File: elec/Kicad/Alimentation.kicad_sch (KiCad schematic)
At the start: 30 parts, among them Q1 SI2323DS-T1, Q4 SI2323DS-T1, SW4 SW_ON/OFF

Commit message: push de magouille pour charles
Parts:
- removed Q4: SI2323DS-T1, Package_TO_SOT_SMD:SOT-23, symbol Transistor_FET:AO3401A
- added D7: 1N4148WS, Diode_SMD:D_SOD-323, symbol Diode:1N4148WS
- R12: value 10 -> 110K
- R18: value 10 -> 300K
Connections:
- net Vbat: now also R12.2
- net VinBat: now also D7.2 (A)
- net at Q1.3 (D), SW4.1 (A): now also D7.1 (K)
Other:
- note added: "MOSFET N-Channel: Si une tension appliqué a la Gate est suppérieur que celle a la Source, le courant va circuler du Drain a la Source"
- note added: "MOSFET P-Channel: Si une tension appliqué a la Gate est inférieur a celle de la Source, le courant va circuler de la Source au Drain"
- note added: "Quand Vbat = 3.5V, BAT_PERCENT = 2.55V Quand Vbat = 4.2V, BAT_PERCENT = 3.07V"
- note removed: "PAS LE BON TYPE DE MOSFET"
- moved on the sheet: R12, R18, SW4

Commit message: va falloir faire le PCB soon
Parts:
- added JP2: USB_ID, symbol Jumper:SolderJumper_2_Open
- added JP2: USB_SHIELD, symbol Jumper:SolderJumper_2_Open
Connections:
- net GND: now also JP2.1 (A), JP2.2 (B)
- net at J?.4 (ID): now also JP2.2 (B)
- net at J?.6 (Shield): now also JP2.1 (A)
- no-connect marks 2 -> 0
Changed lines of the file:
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@@
 	)
 	(junction
+		(at 171.45 50.8)
+		(diameter 0)
+		(color 0 0 0 0)
+	)
+	(junction
 		(at 44.45 57.15)
 		(diameter 0)
@@
 	)
 	(junction
+		(at 176.53 50.8)
+		(diameter 0)
+		(color 0 0 0 0)
+	)
+	(junction
 		(at 104.14 52.07)
 		(diameter 0)
@@
 		(color 0 0 0 0)
 	)
-	(no_connect
-		(at 161.29 49.53)
-	)
-	(no_connect
-		(at 171.45 43.18)
-	)
 	(wire
 		(pts
@@
 	(wire
 		(pts
+			(xy 168.91 55.88) (xy 171.45 55.88)
+		)
+		(stroke
+			(width 0)
+			(type default)
+		)
+	)
+	(wire
+		(pts
 			(xy 115.57 52.07) (xy 125.73 52.07)
 		)
@@
 	(wire
 		(pts
-			(xy 163.83 50.8) (xy 195.58 50.8)
+			(xy 163.83 50.8) (xy 171.45 50.8)
 		)
 		(stroke
@@
 	(wire
 		(pts
+			(xy 171.45 43.18) (xy 176.53 43.18)
+		)
+		(stroke
+			(width 0)
+			(type default)
+		)
+	)
+	(wire
+		(pts
 			(xy 104.14 67.31) (xy 104.14 71.12)
 		)
@@
 	(wire
 		(pts
+			(xy 176.53 50.8) (xy 195.58 50.8)
+		)
+		(stroke
+			(width 0)
+			(type default)
+		)
+	)
+	(wire
+		(pts
 			(xy 100.33 134.62) (xy 113.03 134.62)
 		)
@@
 		)
 	)
+	(wire
+		(pts
+			(xy 171.45 50.8) (xy 176.53 50.8)
+		)
+		(stroke
+			(width 0)
+			(type default)
+		)
+	)
 	(polyline
 		(pts
@@
 	(wire
 		(pts
-			(xy 161.29 48.26) (xy 161.29 49.53)
+			(xy 161.29 48.26) (xy 161.29 55.88)
 		)
 		(stroke
@@
 	(wire
 		(pts
+			(xy 171.45 55.88) (xy 171.45 50.8)
+		)
+		(stroke
+			(width 0)
+			(type default)
+		)
+	)
+	(wire
+		(pts
 			(xy 91.44 160.02) (xy 91.44 161.29)
 		)
@@
 	)
 	(symbol
+		(lib_id "Jumper:SolderJumper_2_Open")
+		(at 176.53 46.99 90)
+		(unit 1)
+		(exclude_from_sim yes)
+		(in_bom no)
+		(on_board yes)
+		(dnp no)
+		(property "Reference" "JP2"
+			(at 181.61 46.736 0)
+			(effects
+				(font
+					(size 1.27 1.27)
+				)
+			)
+		)
+		(property "Value" "USB_ID"
+			(at 179.07 46.482 0)
+			(effects
+				(font
+					(size 1.27 1.27)
+				)
+			)
+		)
+		(property "Footprint" ""
+			(at 176.53 46.99 0)
+			(effects
+				(font
+					(size 1.27 1.27)
+				)
+				(hide yes)
+			)
+		)
+		(property "Datasheet" "~"
+			(at 176.53 46.99 0)
+			(effects
+				(font
+					(size 1.27 1.27)
+				)
+				(hide yes)
+			)
+		)
+		(property "Description" "Solder Jumper, 2-pole, open"
+			(at 176.53 46.99 0)
+			(effects
+				(font
+					(size 1.27 1.27)
+				)
+				(hide yes)
+			)
+		)
+		(pin "2"
+		)
+		(pin "1"
+		)
+		(instances
+			(project "rulerSchematic"
+				(path "/a1545928-1195-40b9-b3c4-78f837012afb/47f0fc71-ff78-496f-bb04-036a9aeaa71c/6f59428e-8e72-4854-8d86-784df1ffb46d"
+					(reference "JP2")
+					(unit 1)
+				)
+			)
+		)
+	)
+	(symbol
 		(lib_id "Device:R")
 		(at 236.22 113.03 180)
@@
 					(unit 1)
 				)
+			)
+		)
+	)
+	(symbol
+		(lib_id "Jumper:SolderJumper_2_Open")
+		(at 165.1 55.88 0)
+		(unit 1)
+		(exclude_from_sim yes)
+		(in_bom no)
+		(on_board yes)
+		(dnp no)
+		(property "Reference" "JP2"
+			(at 165.354 60.96 0)
+			(effects
+				(font
+					(size 1.27 1.27)
+				)
+			)
+		)
+		(property "Value" "USB_SHIELD"
+			(at 165.608 58.42 0)
+			(effects
+				(font
+					(size 1.27 1.27)
+				)
+			)
+		)
+		(property "Footprint" ""
+			(at 165.1 55.88 0)
+			(effects
+				(font
+					(size 1.27 1.27)
+				)
+				(hide yes)
+			)
+		)
+		(property "Datasheet" "~"
+			(at 165.1 55.88 0)
+			(effects
+				(font
+					(size 1.27 1.27)
+				)
+				(hide yes)
+			)
+		)
+		(property "Description" "Solder Jumper, 2-pole, open"
+			(at 165.1 55.88 0)
+			(effects
+				(font
+					(size 1.27 1.27)
+				)
+				(hide yes)
+			)
+		)
+		(pin "2"
+		)
+		(pin "1"
+		)
+		(instances
+			(project ""
+				(path "/a1545928-1195-40b9-b3c4-78f837012afb/47f0fc71-ff78-496f-bb04-036a9aeaa71c/6f59428e-8e72-4854-8d86-784df1ffb46d"
+					(reference "JP2")
+					(unit 1)
+				)

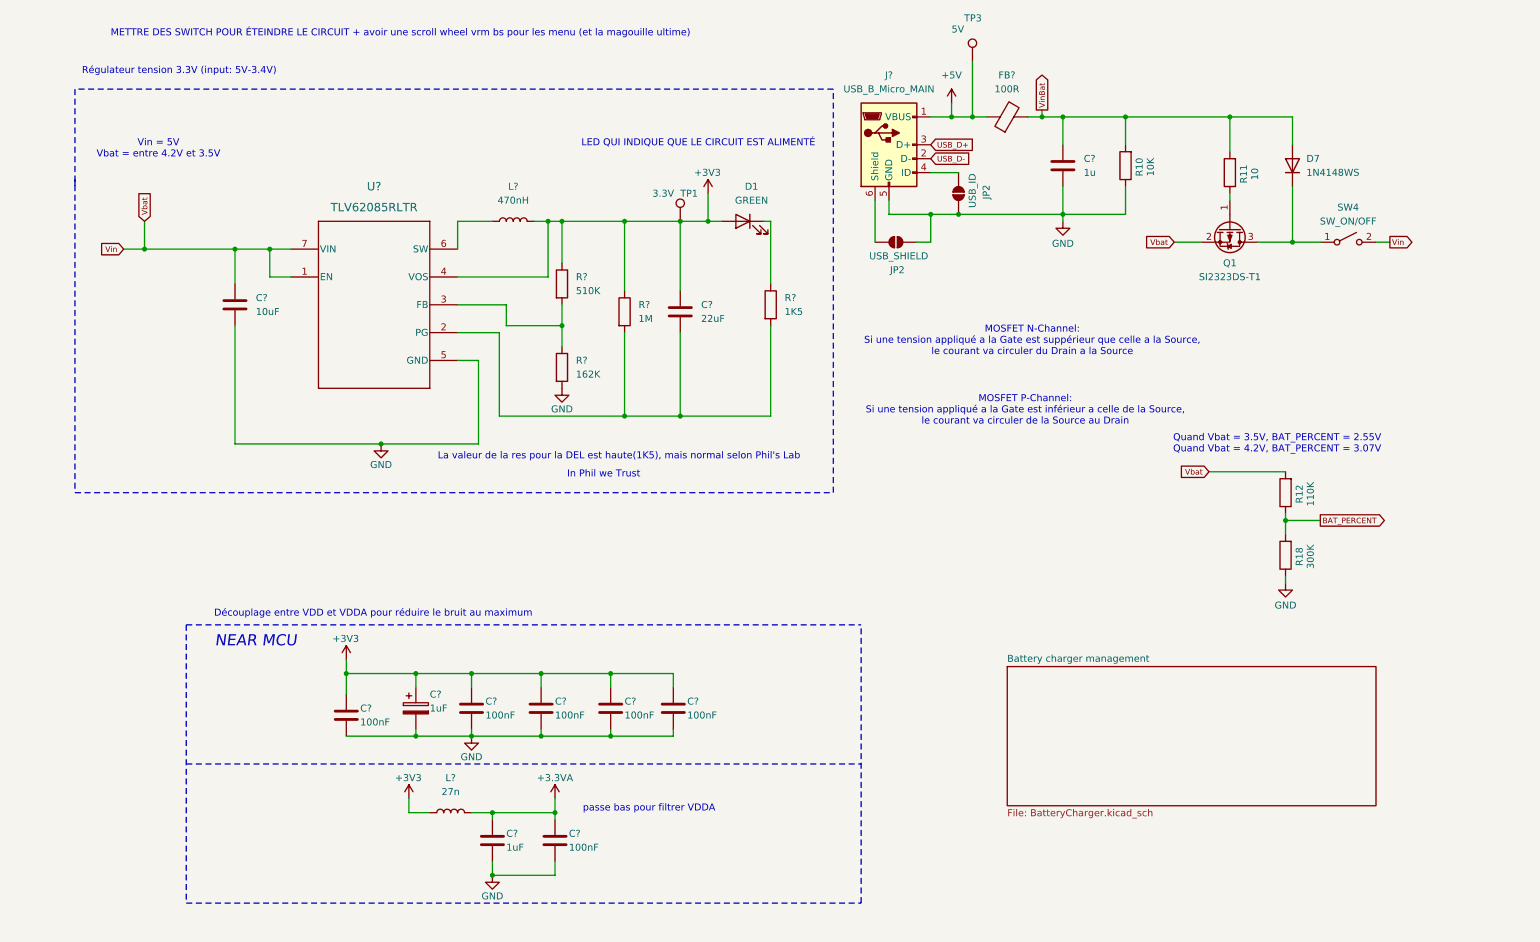
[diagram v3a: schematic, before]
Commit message: add a few footprint
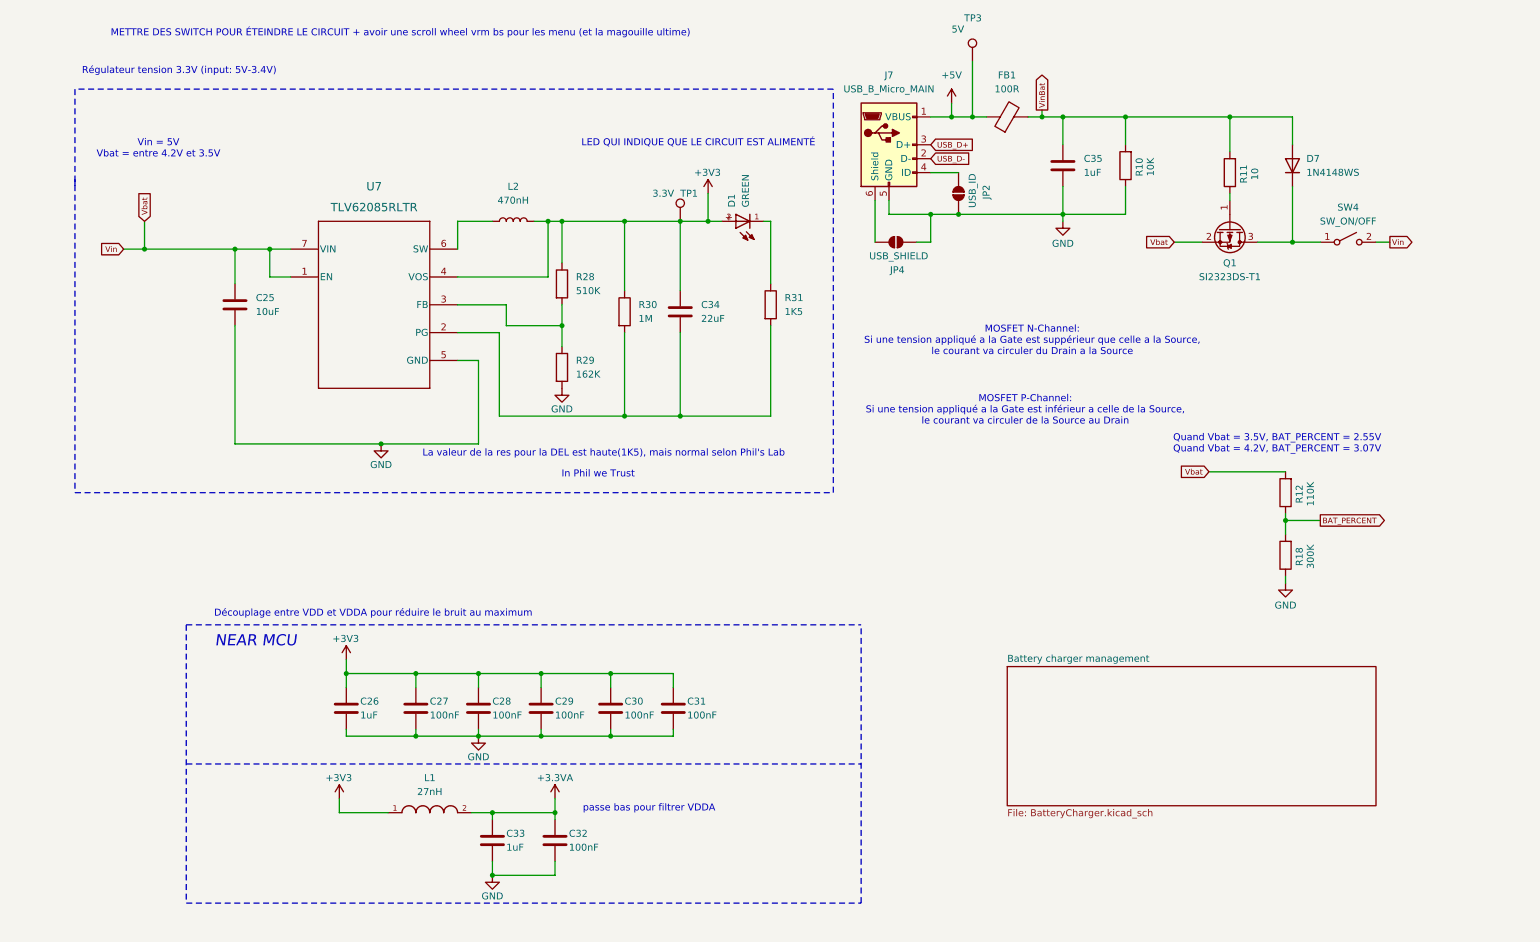
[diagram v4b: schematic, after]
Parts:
- removed C? (x4): 100nF, symbol Device:C
- removed C?: 1uF, symbol Device:C_Polarized
- removed D1: GREEN, symbol Device:LED
- removed JP2: USB_SHIELD, symbol Jumper:SolderJumper_2_Open
- removed L?: 27n, symbol Device:L
- added C26: 1uF, Capacitor_SMD:C_0603_1608Metric_Pad1.08x0.95mm_HandSolder, symbol Device:C
- added C27, C29, C30, C31: 100nF, Capacitor_SMD:C_0603_1608Metric_Pad1.08x0.95mm_HandSolder, symbol Device:C
- added D1: GREEN, SMD_LED_0603:WL-SMCD_0603, symbol WL-SMCD_0603:WL-SMCD_0603
- added JP4: USB_SHIELD, Jumper:SolderJumper-2_P1.3mm_Open_TrianglePad1.0x1.5mm, symbol Jumper:SolderJumper_2_Open
- added L1: 27nH, LQP03TN27NJ02D:INDC0603X33N, symbol LQP03TN27NJ02D:LQP03TN27NJ02D
- C25, C28, C32, C33, C34: renamed from C?; footprint (none) -> Capacitor_SMD:C_0603_1608Metric_Pad1.08x0.95mm_HandSolder
- C35: renamed from C?; value 1u -> 1uF; footprint (none) -> Capacitor_SMD:C_0603_1608Metric_Pad1.08x0.95mm_HandSolder
- FB1: renamed from FB?; footprint (none) -> SMD_FERRITE_BEAD_BLM18EG101TN1D:BEADC1608X65N
- J7: renamed from J?; footprint (none) -> Connector_USB:USB_Micro-B_Amphenol_10103594-0001LF_Horizontal
- JP2: footprint (none) -> Jumper:SolderJumper-2_P1.3mm_Open_TrianglePad1.0x1.5mm
- L2: renamed from L?; footprint (none) -> VLS252012HBX_R47M_1:IND_VLS252012HBX-R47M-1
- R10, R11, R12, R18: footprint (none) -> Resistor_SMD:R_0603_1608Metric_Pad0.98x0.95mm_HandSolder
- R28, R29, R30, R31: renamed from R?; footprint (none) -> Resistor_SMD:R_0603_1608Metric_Pad0.98x0.95mm_HandSolder
- SW4: footprint (none) -> SINGLE_DIP_SWITCH:SW_DS04-254-2-01BK-SMT
- TP1, TP3: footprint (none) -> TestPoint:TestPoint_Loop_D1.80mm_Drill1.0mm_Beaded
- U7: renamed from U?; footprint RLT0007A -> TLV62085RLTR:RLT0007A
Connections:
- net +3.3VA: now also L1.2
- net +3V3: now also C26.1, C27.1, C29.1, C30.1, C31.1, D1.2, L1.1
- net GND: now also C26.2, C27.2, C29.2, C30.2, C31.2, JP4.2 (B)
- net at R31.1: now also D1.1
- net at J7.6 (Shield): now also JP4.1 (A)
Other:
- moved on the sheet: C28

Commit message: formation torture
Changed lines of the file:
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@@
-	)
-	(symbol
-		(lib_id "power:+3.3VA")
-		(at 102.87 157.48 0)
-		(unit 1)
-		(exclude_from_sim no)
-		(in_bom yes)
-		(on_board yes)
-		(dnp no)
-		(property "Reference" "#PWR0111"
-			(at 102.87 161.29 0)
-			(effects
-				(font
-					(size 1.27 1.27)
-				)
-				(hide yes)
-			)
-		)
-		(property "Value" "+3.3VA"
-			(at 102.87 153.67 0)
-			(effects
-				(font
-					(size 1.27 1.27)
-				)
-			)
-		)
-		(property "Footprint" ""
-			(at 102.87 157.48 0)
-			(effects
-				(font
-					(size 1.27 1.27)
-				)
-				(hide yes)
-			)
-		)
-		(property "Datasheet" ""
-			(at 102.87 157.48 0)
-			(effects
-				(font
-					(size 1.27 1.27)
-				)
-				(hide yes)
-			)
-		)
-		(property "Description" ""
-			(at 102.87 157.48 0)
-			(effects
-				(font
-					(size 1.27 1.27)
-				)
-				(hide yes)
-			)
-		)
-		(pin "1"
-		)
-		(instances
-			(project "rulerSchematic"
-				(path "/a1545928-1195-40b9-b3c4-78f837012afb/47f0fc71-ff78-496f-bb04-036a9aeaa71c/6f59428e-8e72-4854-8d86-784df1ffb46d"
-					(reference "#PWR0111")
-					(unit 1)
-				)
-			)
-		)
 	)
 	(symbol
@@
 					(unit 1)
 				)
+			)
+		)
+	)
+	(symbol
+		(lib_name "+3.3VA_1")
+		(lib_id "power:+3.3VA")
+		(at 102.87 157.48 0)
+		(unit 1)
+		(exclude_from_sim no)
+		(in_bom yes)
+		(on_board yes)
+		(dnp no)
+		(fields_autoplaced yes)
+		(property "Reference" "#PWR051"
+			(at 102.87 161.29 0)
+			(effects
+				(font
+					(size 1.27 1.27)
+				)
+				(hide yes)
+			)
+		)
+		(property "Value" "+3.3VA"
+			(at 102.87 152.4 0)
+			(effects
+				(font
+					(size 1.27 1.27)
+				)
+			)
+		)
+		(property "Footprint" ""
+			(at 102.87 157.48 0)
+			(effects
+				(font
+					(size 1.27 1.27)
+				)
+				(hide yes)
+			)
+		)
+		(property "Datasheet" ""
+			(at 102.87 157.48 0)
+			(effects
+				(font
+					(size 1.27 1.27)
+				)
+				(hide yes)
+			)
+		)
+		(property "Description" "Power symbol creates a global label with name \"+3.3VA\""
+			(at 102.87 157.48 0)
+			(effects
+				(font
+					(size 1.27 1.27)
+				)
+				(hide yes)
+			)
+		)
+		(pin "1"
+		)
+		(instances
+			(project "rulerSchematic"
+				(path "/a1545928-1195-40b9-b3c4-78f837012afb/47f0fc71-ff78-496f-bb04-036a9aeaa71c/6f59428e-8e72-4854-8d86-784df1ffb46d"
+					(reference "#PWR051")
+					(unit 1)
+				)

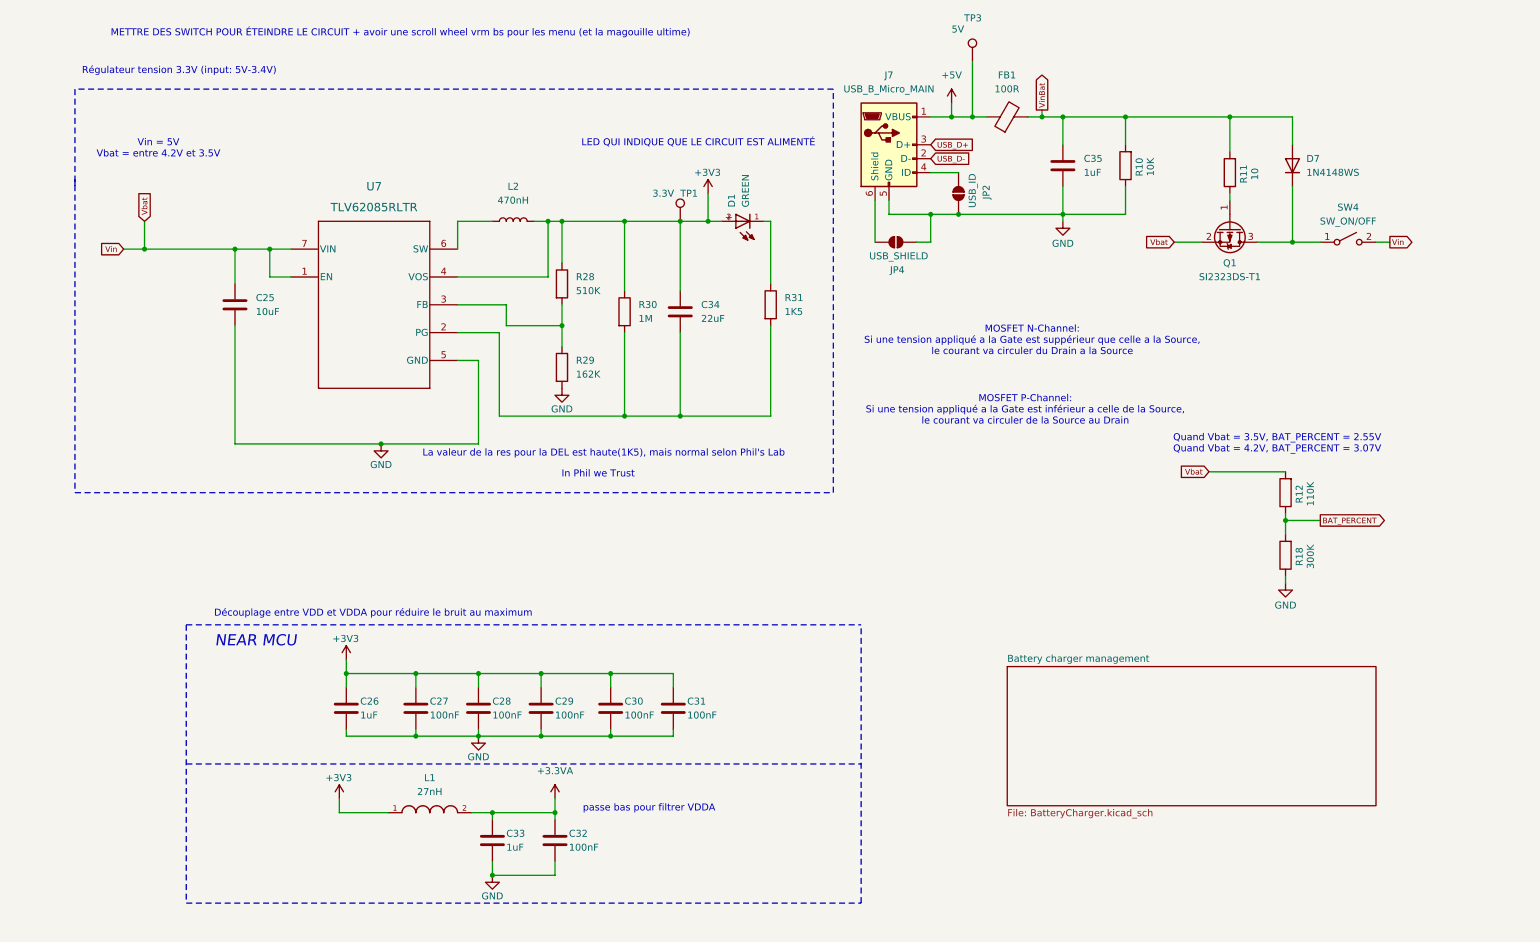
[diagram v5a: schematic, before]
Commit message: J'ai ajouter des power Flag pour spécifier a Kicad que c'est chill (faut qu'il apprenne a ce géré quand même)
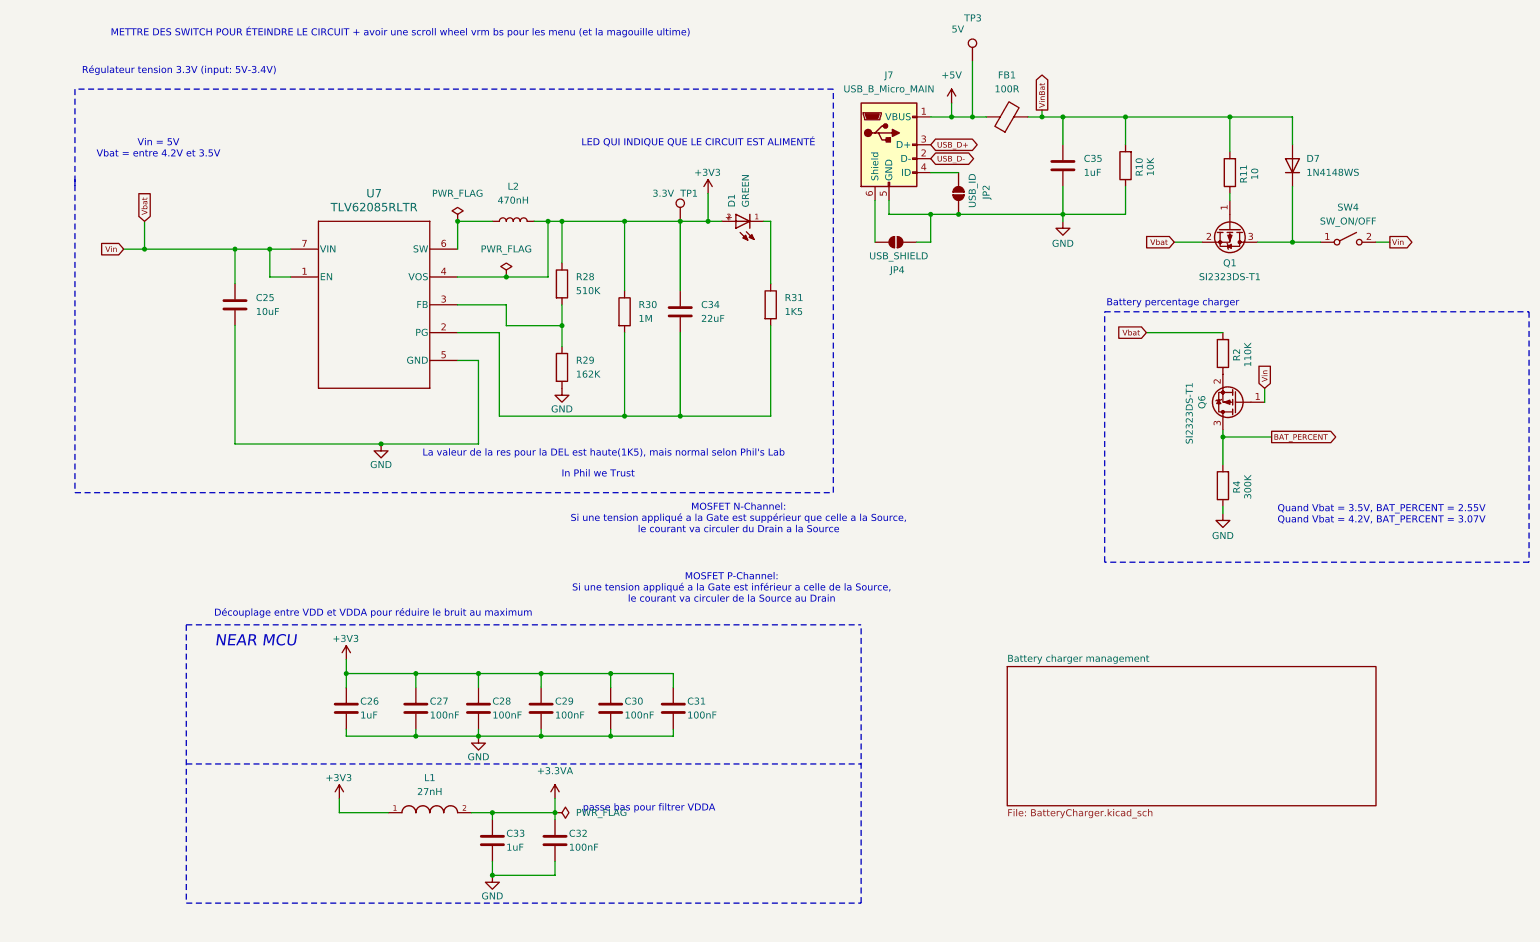
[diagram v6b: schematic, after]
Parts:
- removed R12: 110K, Resistor_SMD:R_0603_1608Metric_Pad0.98x0.95mm_HandSolder, symbol Device:R
- removed R18: 300K, Resistor_SMD:R_0603_1608Metric_Pad0.98x0.95mm_HandSolder, symbol Device:R
- added Q6: SI2323DS-T1, Package_TO_SOT_SMD:SOT-23, symbol Transistor_FET:AO3401A
- added R2: 110K, Resistor_SMD:R_0603_1608Metric_Pad0.98x0.95mm_HandSolder, symbol Device:R
- added R4: 300K, Resistor_SMD:R_0603_1608Metric_Pad0.98x0.95mm_HandSolder, symbol Device:R
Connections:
- net BAT_PERCENT: now also Q6.3 (D), R4.2
- net GND: now also R4.1
- net Vbat: now also Q6.1 (G), R2.2
- new net: Q6.2 (S), R2.1
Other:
- note added: "Battery percentage charger"
